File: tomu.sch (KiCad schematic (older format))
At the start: 15 parts, among them P1 DEBUG, P3 USB-PCB, U1 MKL27Z256VFM4, U2 ateccXXXa

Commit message: Another temp commit.
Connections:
- net +3V3: no longer D1.2 (A)
- net ASPI_MISO: now also U1.1 (PTE0); no longer U1.32 (PTD7)
- net GND: now also D1.1 (K), U1.32 (PTD7)
- net at R1.2: now also D1.2 (A); no longer D1.1 (K)
- no-connect marks 5 -> 4
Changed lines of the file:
@@
 F 3 "" H 860 3510 50  0000 C CNN
 	1    860  3510
-	0    1    1    0
+	0    1    -1   0
 $EndComp
 $Comp
@@
 L +3V3 #PWR05
 U 1 1 579B6568
-P 985 3760
-F 0 "#PWR05" H 985 3610 50  0001 C CNN
-F 1 "+3V3" H 985 3900 50  0000 C CNN
-F 2 "" H 985 3760 50  0000 C CNN
-F 3 "" H 985 3760 50  0000 C CNN
-	1    985  3760
+P 1085 3770
+F 0 "#PWR05" H 1085 3620 50  0001 C CNN
+F 1 "+3V3" H 1085 3920 50  0000 C CNN
+F 2 "" H 1085 3770 50  0000 C CNN
+F 3 "" H 1085 3770 50  0000 C CNN
+	1    1085 3770
 	-1   0    0    1
 $EndComp
@@
 Text Label 2925 4775 2    39   ~ 0
 ASPI_MOSI
-Text Label 2925 4875 2    39   ~ 0
+Text Label 1010 4840 0    39   ~ 0
 ASPI_MISO
 Wire Wire Line
@@
 Connection ~ 5455 3025
 Wire Wire Line
-	985  3760 985  3710
-Wire Wire Line
-	860  3710 1085 3710
-Connection ~ 985  3710
-Wire Wire Line
 	1260 3260 1085 3260
 Wire Wire Line
@@
 Connection ~ 1520 5325
 Wire Wire Line
-	2610 4875 2610 5605
-Wire Wire Line
-	2610 4875 2935 4875
+	2850 4875 2935 4875
 Wire Wire Line
 	2530 4775 2530 5040
@@
 	2220 4740 2255 4740
 Wire Wire Line
-	2610 5605 1125 5605
-Wire Wire Line
-	1125 5605 1125 4840
-Wire Wire Line
-	1125 4840 1320 4840
+	1010 4840 1320 4840
 Text Notes 2970 3675 2    20   ~ 0
 SCL
@@
 Wire Notes Line
 	2135 3410 2070 3410
-NoConn ~ 3935 3300
 NoConn ~ 3935 3400
+Text Label 3875 3300 2    39   ~ 0
+ASPI_MISO
+Wire Wire Line
+	3935 3300 3875 3300
+$Comp
+L GND #PWR09
+U 1 1 5839545D
+P 2850 4875
+F 0 "#PWR09" H 2850 4625 50  0001 C CNN
+F 1 "GND" H 2850 4725 50  0000 C CNN
+F 2 "" H 2850 4875 50  0000 C CNN
+F 3 "" H 2850 4875 50  0000 C CNN
+	1    2850 4875
+	1    0    0    -1
+$EndComp
+Wire Wire Line
+	1085 3770 1085 3710
+$Comp
+L GND #PWR?
+U 1 1 583958AE
+P 860 3765
+F 0 "#PWR?" H 860 3515 50  0001 C CNN
+F 1 "GND" H 860 3615 50  0000 C CNN
+F 2 "" H 860 3765 50  0000 C CNN
+F 3 "" H 860 3765 50  0000 C CNN
+	1    860  3765
+	1    0    0    -1
+$EndComp
+Wire Wire Line
+	860  3765 860  3710
 $EndSCHEMATC

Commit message: More improvements.
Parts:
- added JP1: Jumper_NO_Small, Resistors_SMD:R_0402, symbol Jumper_NO_Small
- U2: footprint (none) -> Housings_DFN_QFN:DFN-8-1EP_3x2mm_Pitch0.5mm
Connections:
- net +3V3: now also D1.2 (A)
- net GND: no longer D1.1 (K)
- net at R1.2: now also D1.1 (K); no longer D1.2 (A)
- net ASPI_CS renamed ASPI_CS1
- net ASPI_CS1: now also JP1.2; no longer U2.1 (CS)
- new net ASPI_CS2: JP1.1, U2.1 (CS)

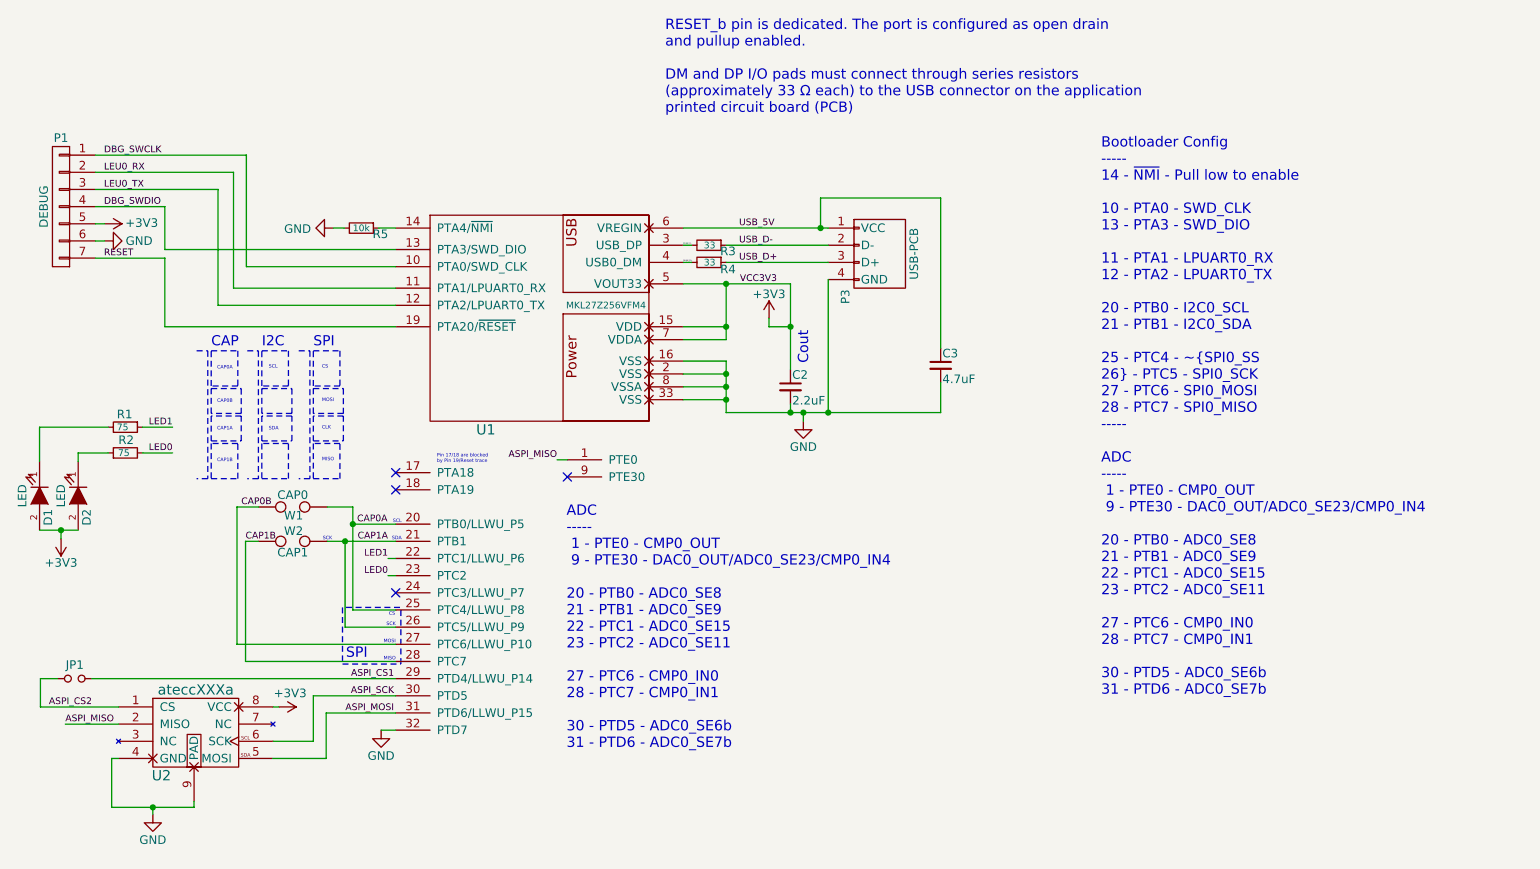
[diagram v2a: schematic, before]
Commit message: Fully routed design which passes DRC.
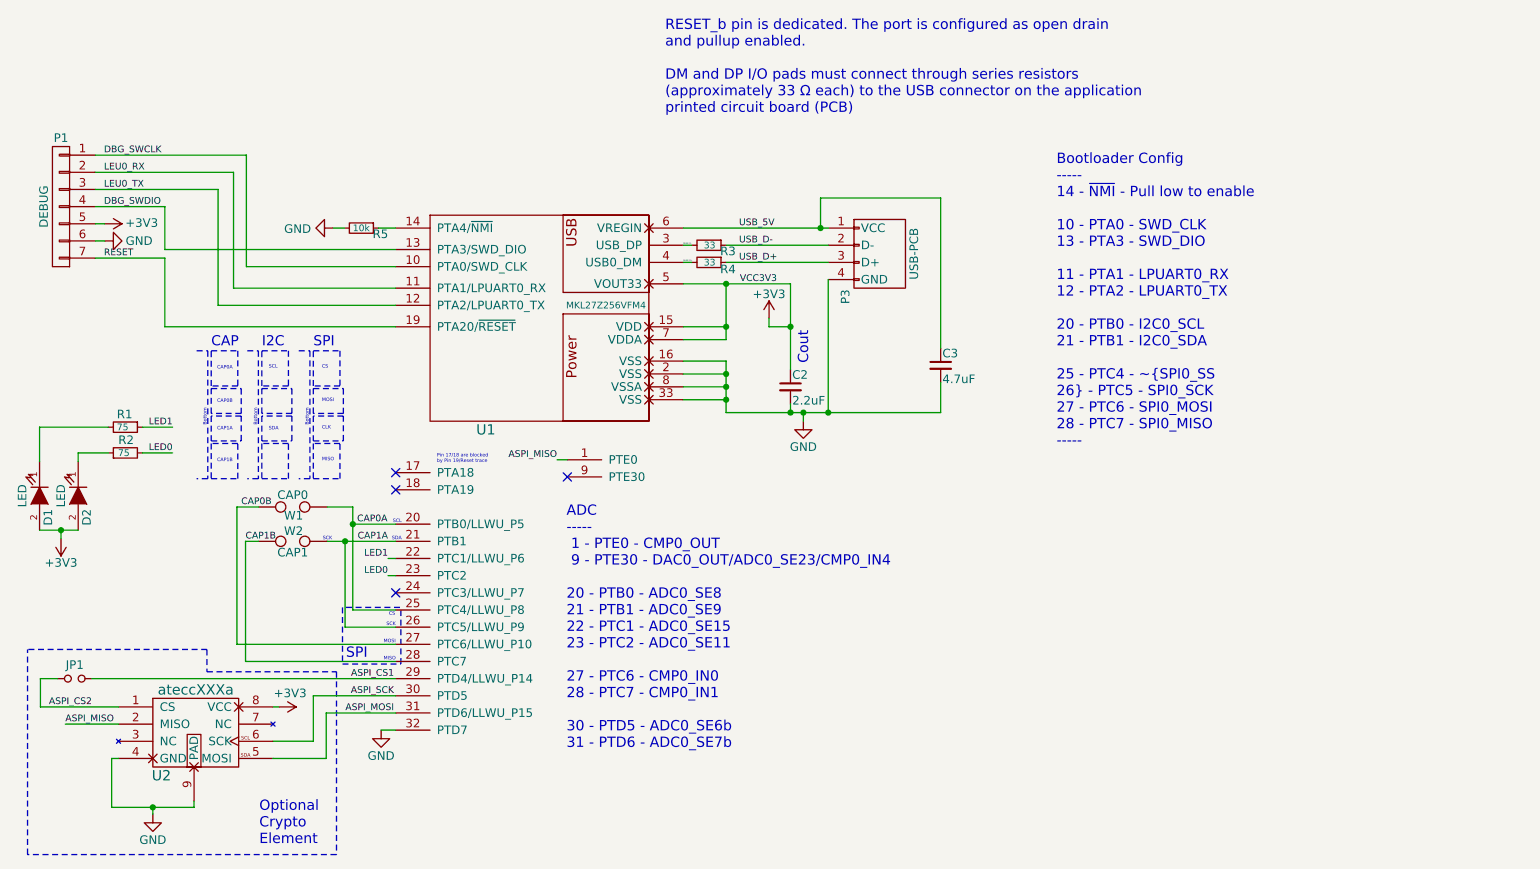
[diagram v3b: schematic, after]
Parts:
- W1, W2: footprint Measurement_Points:Test_Point_2Pads -> usb-pcb:cap-points
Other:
- note added: "Bootloader Config\n-----\n14 - ~NMI~ - Pull low to enable\n\n10 - PTA0 - SWD_CLK\n13 - PTA3 - SWD_DIO\n\n11 - PTA1 - LPUART0_RX\n12 - PTA2 - LPUART0_TX\n\n20 - PTB0 - I2C0_SCL\n21 - PTB1 - I2C0_SDA\n\n25 - PTC4 - ~SPI0_SS\n26 - PTC5 - SPI0_SCK\n27 - PTC6 - SPI0_MOSI\n28 - PTC7 - SPI0_MISO\n-----"
- note added: "Bottom"
- note added: "Optional\nCrypto\nElement"
- note removed: "Bootloader Config\n-----\n14 - ~NMI~ - Pull low to enable\n\n10 - PTA0 - SWD_CLK\n13 - PTA3 - SWD_DIO\n\n11 - PTA1 - LPUART0_RX\n12 - PTA2 - LPUART0_TX\n\n20 - PTB0 - I2C0_SCL\n21 - PTB1 - I2C0_SDA\n\n25 - PTC4 - ~SPI0_SS\n26 - PTC5 - SPI0_SCK\n27 - PTC6 - SPI0_MOSI\n28 - PTC7 - SPI0_MISO\n-----\n\nADC \n-----\n 1 - PTE0 - CMP0_OUT\n 9 - PTE30 - DAC0_OUT/ADC0_SE23/CMP0_IN4\n\n20 - PTB0 - ADC0_SE8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"
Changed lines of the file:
@@
 F 0 "W1" H 2330 3525 50  0000 C CNN
 F 1 "CAP0" H 2335 3645 50  0000 C CNN
-F 2 "Measurement_Points:Test_Point_2Pads" H 2335 3575 50  0001 C CNN
+F 2 "usb-pcb:cap-points" H 2335 3575 50  0001 C CNN
 F 3 "" H 2335 3575 50  0000 C CNN
 	1    2335 3575
@@
 F 0 "W2" H 2330 3835 50  0000 C CNN
 F 1 "CAP1" H 2335 3710 50  0000 C CNN
-F 2 "Measurement_Points:Test_Point_2Pads" H 2335 3775 50  0001 C CNN
+F 2 "usb-pcb:cap-points" H 2335 3775 50  0001 C CNN
 F 3 "" H 2335 3775 50  0000 C CNN
 	1    2335 3775
 	-1   0    0    -1
 $EndComp
-Text Notes 7045 4680 0    60   ~ 0
-Bootloader Config\n-----\n14 - ~NMI~ - Pull low to enable\n\n10 - PTA0 - SWD_CLK\n13 - PTA3 - SWD_DIO\n\n11 - PTA1 - LPUART0_RX\n12 - PTA2 - LPUART0_TX\n\n20 - PTB0 - I2C0_SCL\n21 - PTB1 - I2C0_SDA\n\n25 - PTC4 - ~SPI0_SS\n26 - PTC5 - SPI0_SCK\n27 - PTC6 - SPI0_MOSI\n28 - PTC7 - SPI0_MISO\n-----\n\nADC \n-----\n 1 - PTE0 - CMP0_OUT\n 9 - PTE30 - DAC0_OUT/ADC0_SE23/CMP0_IN4\n\n20 - PTB0 - ADC0_SE8\n21 - PTB1 - ADC0_SE9\n22 - PTC1 - ADC0_SE15\n23 - PTC2 - ADC0_SE11\n\n27 - PTC6 - CMP0_IN0\n28 - PTC7 - CMP0_IN1\n\n30 - PTD5 - ADC0_SE6b\n31 - PTD6 - ADC0_SE7b
+Text Notes 6785 3230 0    60   ~ 0
+Bootloader Config\n-----\n14 - ~NMI~ - Pull low to enable\n\n10 - PTA0 - SWD_CLK\n13 - PTA3 - SWD_DIO\n\n11 - PTA1 - LPUART0_RX\n12 - PTA2 - LPUART0_TX\n\n20 - PTB0 - I2C0_SCL\n21 - PTB1 - I2C0_SDA\n\n25 - PTC4 - ~SPI0_SS\n26 - PTC5 - SPI0_SCK\n27 - PTC6 - SPI0_MOSI\n28 - PTC7 - SPI0_MISO\n-----
 Text Label 2710 3675 0    39   ~ 0
 CAP0A
@@
 Wire Wire Line
 	865  4575 965  4575
+Text Notes 2430 3105 1    20   ~ 0
+Bottom
+Text Notes 2130 3105 1    20   ~ 0
+Bottom
+Text Notes 1835 3105 1    20   ~ 0
+Bottom
+Wire Notes Line
+	795  4405 1835 4405
+Wire Notes Line
+	1835 4405 1835 4535
+Wire Notes Line
+	1835 4535 2590 4535
+Wire Notes Line
+	2590 4535 2590 5600
+Wire Notes Line
+	2590 5600 790  5600
+Wire Notes Line
+	790  5600 790  4405
+Text Notes 2140 5550 0    60   ~ 0
+Optional\nCrypto\nElement
 $EndSCHEMATC
